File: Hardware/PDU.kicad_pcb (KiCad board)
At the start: 4 copper layers, 65.5 x 50 mm, 150 parts, among them IC1 SiC437AED-T1-GE3, J1 Conn_01x03_MountingPin, J10 USB_C_Receptacle_USB2.0, J2 Conn_01x04_Male, J3 XT60PW-M, J4 XT60PW-M, J5 Conn_01x02_Male, J6 Conn_01x08_Male, J7 FAN, J8 XT60PW-F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

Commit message: feat: R28
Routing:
- net Net-(J8-Pad1): track 9.05 -> 9.85 mm
- net /Switches+RBUS/Fuse_OUT: track 22.5 -> 23.2 mm

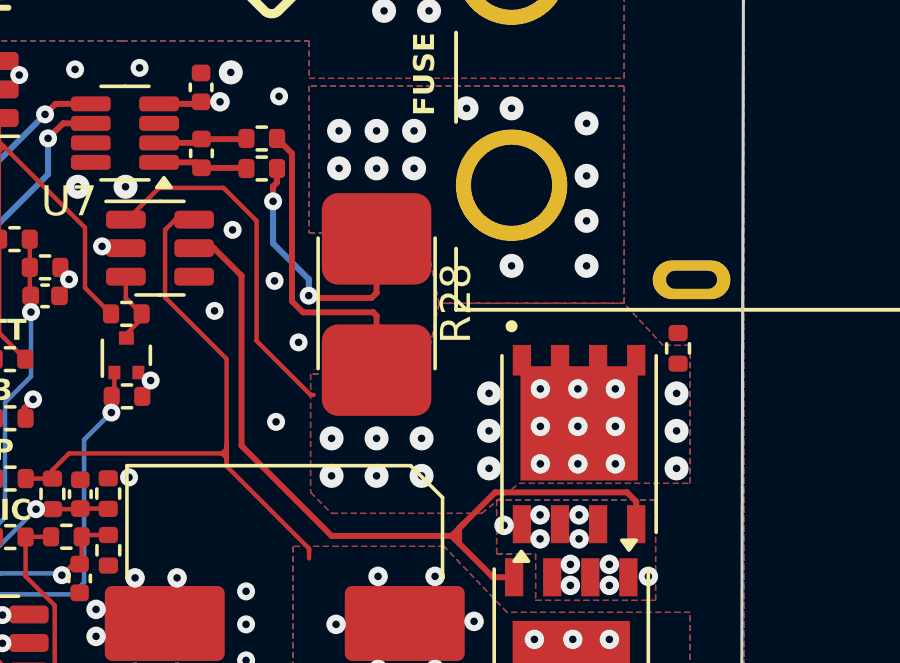
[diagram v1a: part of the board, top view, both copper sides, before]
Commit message: feat: Changed mosfet to non deprecated version
Higher input voltage too: SI7135DP-T1-GE3
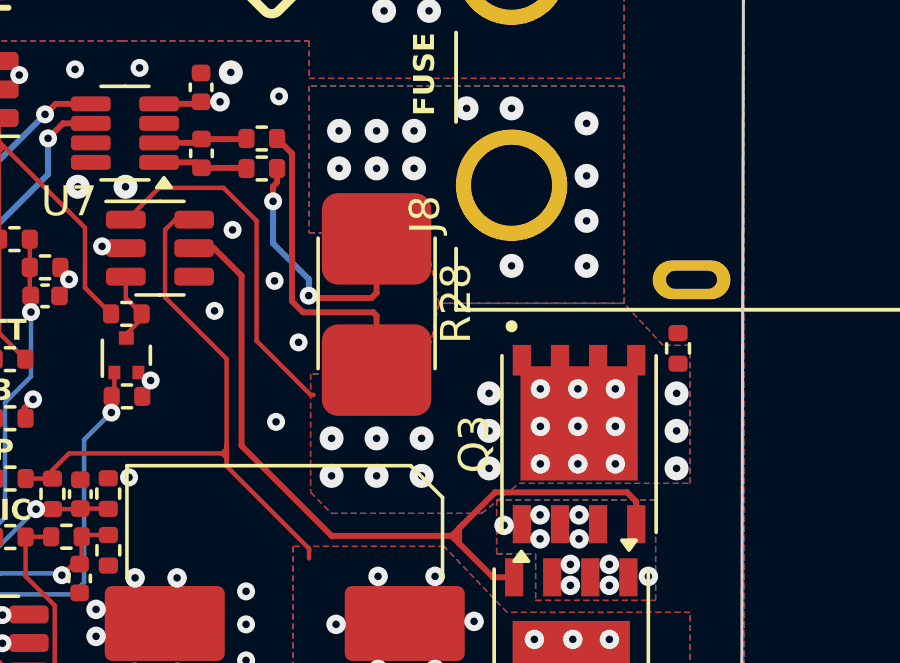
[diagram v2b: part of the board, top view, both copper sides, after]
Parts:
- Q3, Q4: value SI7635DP-T1-GE3 -> SI7135DP-T1-GE3
